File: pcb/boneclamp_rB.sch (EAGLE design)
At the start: 61 parts, among them IC1 24C, U1 AD7656YSTZ, U2 LT1964ES5-5TRMPBF, U3 LT1962EMS8-5PBF, U7 AD7682BCPZ, U8 TPS63700DRCT

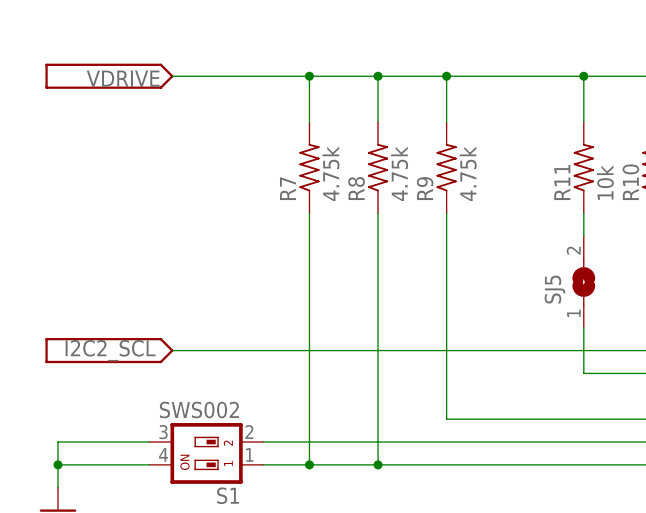
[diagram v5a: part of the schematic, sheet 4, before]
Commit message: Added data sheets for the smd-to-dip adapters we will use. Minor changes to schematic
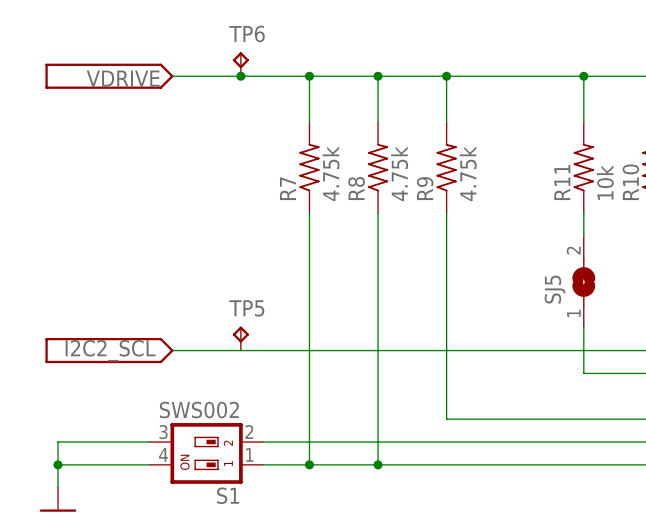
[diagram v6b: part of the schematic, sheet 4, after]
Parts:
- added TP5, TP6: TPB1,27, testpad:TPB1,27
- C6: value 0.01uF -> 10nF
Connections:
- net VDRIVE: now also TP6.TP
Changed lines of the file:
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@@
 <setting verticaltext="up"/>
 </settings>
-<grid distance="0.1" unitdist="inch" unit="inch" style="lines" multiple="1" display="yes" altdistance="0.01" altunitdist="inch" altunit="inch"/>
+<grid distance="0.1" unitdist="inch" unit="inch" style="lines" multiple="1" display="no" altdistance="0.01" altunitdist="inch" altunit="inch"/>
 <layers>
 <layer number="1" name="Top" color="4" fill="1" visible="no" active="no"/>
@@
 <part name="SUPPLY9" library="supply2" deviceset="AGND" device=""/>
 <part name="C5" library="rcl" deviceset="C-EU" device="C0805" value="1uF"/>
-<part name="C6" library="rcl" deviceset="C-EU" device="C0805" value="0.01uF"/>
+<part name="C6" library="rcl" deviceset="C-EU" device="C0805" value="10nF"/>
 <part name="C7" library="rcl" deviceset="C-EU" device="C0805" value="10uF"/>
 <part name="U$20" library="boneclamp" deviceset="V_SIG" device=""/>
 <part name="U3" library="linear-extended-01" deviceset="LT1962EMS8-5PBF" device=""/>
+<part name="TP5" library="testpad" deviceset="TP" device="B1,27"/>
+<part name="TP6" library="testpad" deviceset="TP" device="B1,27"/>
 </parts>
 <sheets>
@@
 <instance part="SJ5" gate="1" x="-27.94" y="38.1" rot="R90"/>
 <instance part="U$41" gate="G$1" x="-73.66" y="30.48" rot="R180"/>
+<instance part="TP5" gate="G$1" x="-66.04" y="33.02"/>
+<instance part="TP6" gate="G$1" x="-66.04" y="63.5"/>
 </instances>
 <busses>
@@
 <wire x1="-43.18" y1="60.96" x2="-50.8" y2="60.96" width="0.1524" layer="91"/>
 <wire x1="-50.8" y1="60.96" x2="-58.42" y2="60.96" width="0.1524" layer="91"/>
-<wire x1="-58.42" y1="60.96" x2="-73.66" y2="60.96" width="0.1524" layer="91"/>
+<wire x1="-58.42" y1="60.96" x2="-66.04" y2="60.96" width="0.1524" layer="91"/>
+<wire x1="-66.04" y1="60.96" x2="-73.66" y2="60.96" width="0.1524" layer="91"/>
 <wire x1="5.08" y1="35.56" x2="5.08" y2="60.96" width="0.1524" layer="91"/>
 <junction x="5.08" y="60.96"/>
@@
 <wire x1="-20.32" y1="60.96" x2="-20.32" y2="55.88" width="0.1524" layer="91"/>
 <junction x="-20.32" y="60.96"/>
-</segment>
-</net>
+<pinref part="TP6" gate="G$1" pin="TP"/>
+<junction x="-66.04" y="60.96"/>
+</segment>
+</net>

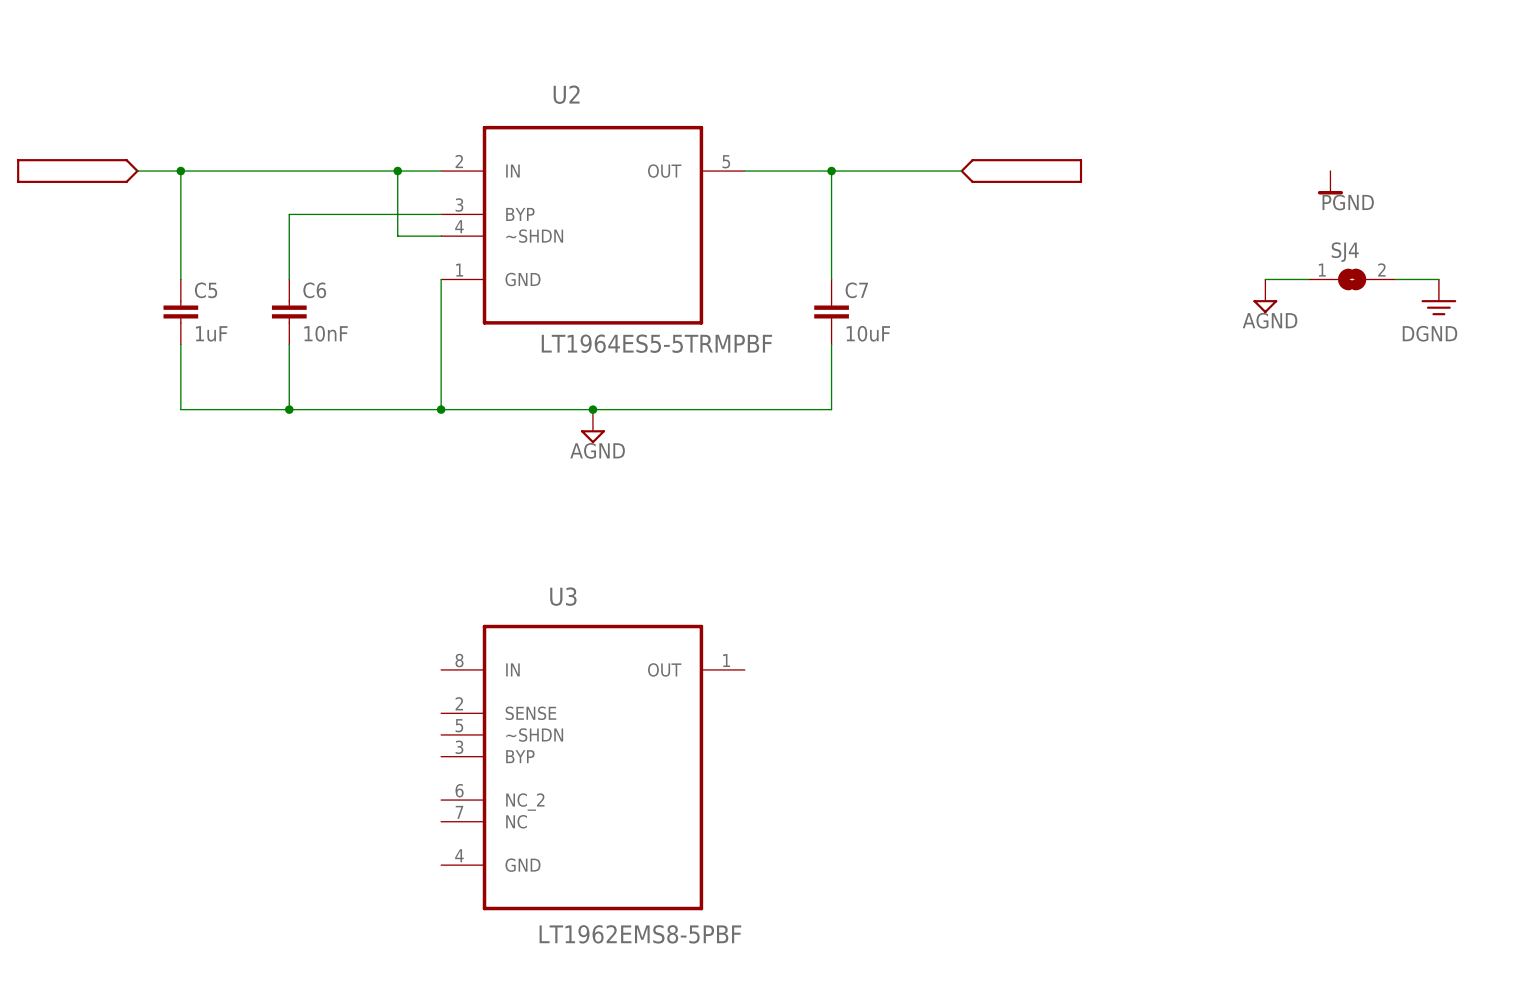
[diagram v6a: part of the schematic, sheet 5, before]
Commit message: Finished power supply circuits on schematic. Updated BOM and added new data sheets.
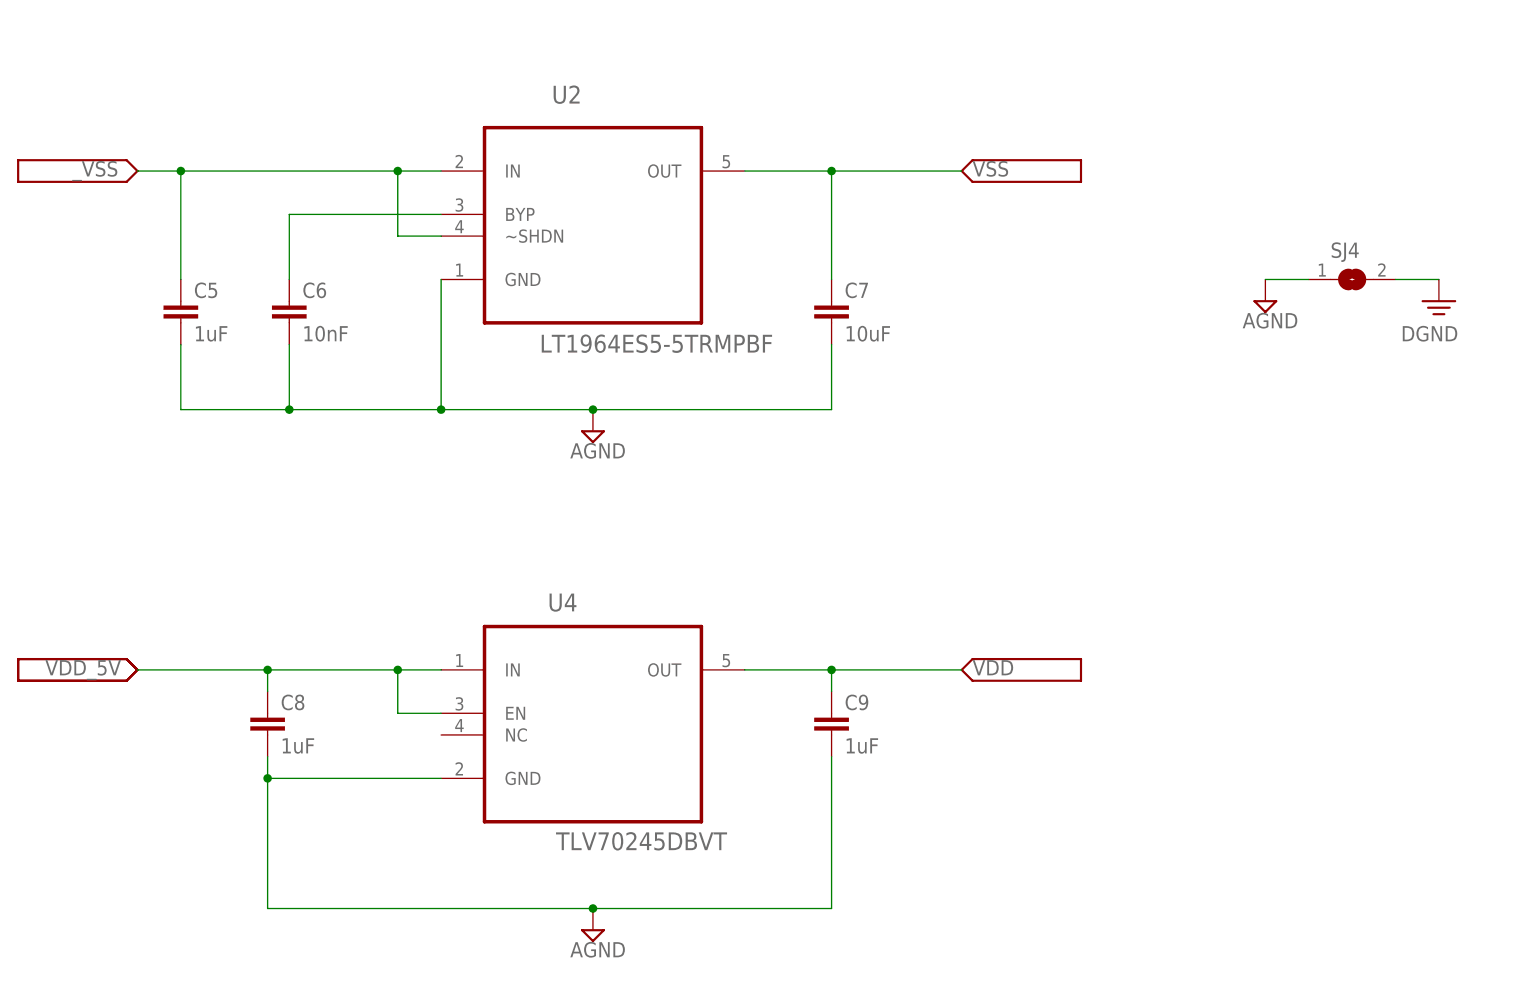
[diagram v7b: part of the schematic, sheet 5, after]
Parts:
- removed U3: LT1962EMS8-5PBF, linear-extended-01:LT1962EMS8-5PBF
- added C8, C9: 1uF, rcl:C-EUC0805
- added U4: TLV70245DBVT, ti-extended:TLV70025DDCR
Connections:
- net AGND: now also C8.2, C9.2, U4.GND
- net VDD: now also C9.1, U4.OUT
- net VDD_5V: now also C8.1, U4.EN, U4.IN
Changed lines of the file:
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@@
 <part name="U$33" library="boneclamp" deviceset="V_SIG" device=""/>
 <part name="U$34" library="boneclamp" deviceset="V_SIG" device=""/>
-<part name="SUPPLY18" library="supply2" deviceset="0V" device="" value="PGND"/>
 <part name="IC1" library="on-semiconductor-01" deviceset="24C*" device=""/>
 <part name="U$36" library="boneclamp" deviceset="V_SIG" device=""/>
@@
 <part name="C7" library="rcl" deviceset="C-EU" device="C0805" value="10uF"/>
 <part name="U$20" library="boneclamp" deviceset="V_SIG" device=""/>
-<part name="U3" library="linear-extended-01" deviceset="LT1962EMS8-5PBF" device=""/>
 <part name="TP5" library="testpad" deviceset="TP" device="B1,27"/>
 <part name="TP6" library="testpad" deviceset="TP" device="B1,27"/>
+<part name="U4" library="ti-extended" deviceset="TLV70025DDCR" device="" value="TLV70245DBVT"/>
+<part name="C8" library="rcl" deviceset="C-EU" device="C0805" value="1uF"/>
+<part name="C9" library="rcl" deviceset="C-EU" device="C0805" value="1uF"/>
+<part name="SUPPLY10" library="supply2" deviceset="AGND" device=""/>
+<part name="U$21" library="boneclamp" deviceset="V_SIG" device=""/>
+<part name="U$22" library="boneclamp" deviceset="V_SIG" device=""/>
+<part name="U$25" library="boneclamp" deviceset="V_SIG" device=""/>
 </parts>
 <sheets>
@@
 <instance part="DGND3" gate="PE" x="99.06" y="-12.7"/>
 <instance part="SUPPLY17" gate="G$1" x="78.74" y="-12.7"/>
-<instance part="SUPPLY18" gate="0V" x="86.36" y="0"/>
 <instance part="U8" gate="A" x="0" y="63.5"/>
 <instance part="U$18" gate="G$1" x="-53.34" y="60.96" rot="R180"/>
@@
 <instance part="C7" gate="G$1" x="27.94" y="-12.7"/>
 <instance part="U$20" gate="G$1" x="43.18" y="2.54"/>
-<instance part="U3" gate="A" x="0" y="-63.5"/>
+<instance part="U4" gate="A" x="0" y="-58.42"/>
+<instance part="C8" gate="G$1" x="-38.1" y="-60.96"/>
+<instance part="C9" gate="G$1" x="27.94" y="-60.96"/>
+<instance part="SUPPLY10" gate="G$1" x="0" y="-86.36"/>
+<instance part="U$21" gate="G$1" x="-53.34" y="-55.88" rot="R180"/>
+<instance part="U$22" gate="G$1" x="-53.34" y="-55.88" rot="R180"/>
+<instance part="U$25" gate="G$1" x="43.18" y="-55.88"/>
 </instances>
 <busses>
@@
 <pinref part="C7" gate="G$1" pin="2"/>
 </segment>
+<segment>
+<pinref part="C9" gate="G$1" pin="2"/>
+<wire x1="27.94" y1="-66.04" x2="27.94" y2="-83.82" width="0.1524" layer="91"/>
+<wire x1="27.94" y1="-83.82" x2="0" y2="-83.82" width="0.1524" layer="91"/>
+<pinref part="SUPPLY10" gate="G$1" pin="AGND"/>
+<pinref part="C8" gate="G$1" pin="2"/>
+<wire x1="-38.1" y1="-66.04" x2="-38.1" y2="-68.58" width="0.1524" layer="91"/>
+<wire x1="-38.1" y1="-68.58" x2="-38.1" y2="-83.82" width="0.1524" layer="91"/>
+<junction x="-38.1" y="-68.58"/>
+<pinref part="U4" gate="A" pin="GND"/>
+<wire x1="-17.78" y1="-68.58" x2="-38.1" y2="-68.58" width="0.1524" layer="91"/>
+<wire x1="0" y1="-83.82" x2="-38.1" y2="-83.82" width="0.1524" layer="91"/>
+<junction x="0" y="-83.82"/>
+</segment>
 </net>
 <net name="DGND" class="0">
@@
 <pinref part="R5" gate="G$1" pin="1"/>
 <wire x1="-45.72" y1="68.58" x2="-45.72" y2="60.96" width="0.1524" layer="91"/>
+</segment>
+<segment>
+<pinref part="U4" gate="A" pin="IN"/>
+<wire x1="-17.78" y1="-55.88" x2="-22.86" y2="-55.88" width="0.1524" layer="91"/>
+<pinref part="C8" gate="G$1" pin="1"/>
+<wire x1="-22.86" y1="-55.88" x2="-38.1" y2="-55.88" width="0.1524" layer="91"/>
+<wire x1="-38.1" y1="-55.88" x2="-53.34" y2="-55.88" width="0.1524" layer="91"/>
+<wire x1="-38.1" y1="-58.42" x2="-38.1" y2="-55.88" width="0.1524" layer="91"/>
+<junction x="-38.1" y="-55.88"/>
+<wire x1="-22.86" y1="-55.88" x2="-22.86" y2="-60.96" width="0.1524" layer="91"/>
+<junction x="-22.86" y="-55.88"/>
+<pinref part="U4" gate="A" pin="EN"/>
+<wire x1="-22.86" y1="-60.96" x2="-17.78" y2="-60.96" width="0.1524" layer="91"/>
+<label x="-64.135" y="-56.515" size="1.778" layer="95"/>
 </segment>
 </net>
@@
 <wire x1="-22.86" y1="-5.08" x2="-22.86" y2="2.54" width="0.1524" layer="91"/>
 <junction x="-22.86" y="2.54"/>
+<label x="-60.96" y="1.905" size="1.778" layer="95"/>
 </segment>
 </net>
@@
 <wire x1="27.94" y1="2.54" x2="43.18" y2="2.54" width="0.1524" layer="91"/>
 <junction x="27.94" y="2.54"/>
-</segment>
-</net>
+<label x="44.45" y="1.905" size="1.778" layer="95"/>
+</segment>
+</net>
+<net name="VDD" class="0">
+<segment>
+<pinref part="U4" gate="A" pin="OUT"/>
+<pinref part="C9" gate="G$1" pin="1"/>
+<wire x1="17.78" y1="-55.88" x2="27.94" y2="-55.88" width="0.1524" layer="91"/>
+<wire x1="27.94" y1="-55.88" x2="27.94" y2="-58.42" width="0.1524" layer="91"/>
+<wire x1="27.94" y1="-55.88" x2="43.18" y2="-55.88" width="0.1524" layer="91"/>
+<junction x="27.94" y="-55.88"/>
+<label x="44.45" y="-56.515" size="1.778" layer="95"/>
+</segment>
+</net>

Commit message: Updated adafruit library with 2X5 0.1 inch pitch header, which we will use for I/O on the BC. Added that to the schematic
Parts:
- removed BCIO: F15-SHEILD, adafruit:F15-SHEILD
- removed JP1: (no value), jumper:JP1E
- added JP5: PINHD-2X5/90, adafruit:PINHD-2X5/90
- added U3, U5, U6, U9: ADA4841-2YRZ, analog-devices-01:ADA4841-2YRZ
- U1: value AD7656YSTZ -> ADA4841-2YRZ; device analog-devices-01:AD7656YSTZ -> analog-devices-01:ADA4841-2YRZ
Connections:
- removed net CONVST: U1.CONVST_A, U1.CONVST_B, U1.CONVST_C
- new net ADC_A: JP5.4
- new net ADC_B: JP5.6
- new net ADC_C: JP5.8
- new net ADC_D: JP5.10
- new net N$15: U3.OUT1, U5.OUT1
- new net N$26: U3.OUT2, U5.OUT2
- net AGND: no longer BCIO.1, JP1.2, U1.AGND, U1.AGND_11, U1.AGND_2, U1.AGND_3, U1.AGND_4, U1.AGND_5, U1.AGND_6, U1.AGND_7, U1.AGND_8, U1.AGND_9
- net DAC_A: now also JP5.3; no longer BCIO.8
- net DAC_B: now also JP5.5; no longer BCIO.9
- net DAC_C: now also JP5.7; no longer BCIO.10
- net DAC_D: now also JP5.9; no longer BCIO.11
- net DGND: no longer U1.DGND, U1.DGND_2
- net N$1: now also U3.+VS, U5.+VS; no longer BCIO.2, U1.V1
- net N$10: no longer U1.REFCAPB
- net N$11: no longer U1.REFCAPC
- net N$12: no longer U1.RANGE
- net N$13: no longer U1.AVCC, U1.AVCC_2, U1.AVCC_3, U1.AVCC_4, U1.AVCC_5, U1.AVCC_6, U1.AVCC_7, U1.AVCC_8
- net N$2: now also U3.+IN1, U5.+IN1; no longer BCIO.3, U1.V2
- net N$20: no longer U1.REFIN/REFOUT
- net N$3: now also U3.-IN1, U5.-IN1; no longer BCIO.4, U1.V3
- net N$4: now also U3.+IN2, U5.+IN2; no longer BCIO.5, U1.V4
- net N$5: now also U3.-IN2, U5.-IN2; no longer BCIO.6, U1.V5
- net N$6: now also U3.-VS, U5.-VS; no longer BCIO.7, U1.V6
- net SGND: now also JP5.1, JP5.2; no longer BCIO.P$1, BCIO.P$2, JP1.1
- net VSS: no longer U1.VSS
